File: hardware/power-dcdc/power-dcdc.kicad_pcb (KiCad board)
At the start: 2 copper layers, 110 x 70 mm, 67 parts, among them J1 SOLAR_IN, J2 BATT2, J3 BATT1, J4 DCDC-MEASURES, J5 DCDC-PWM, Q1 SIR164ADP, Q2 SIR164ADP, Q3 SI7149ADP, Q4 SI7149ADP, Q5 SI7149ADP, Q6 SI7149ADP, U1 LP4951C, U2 NCP5901B, U3 PAC1953-1, U4 DGD0215, U5 DGD0215

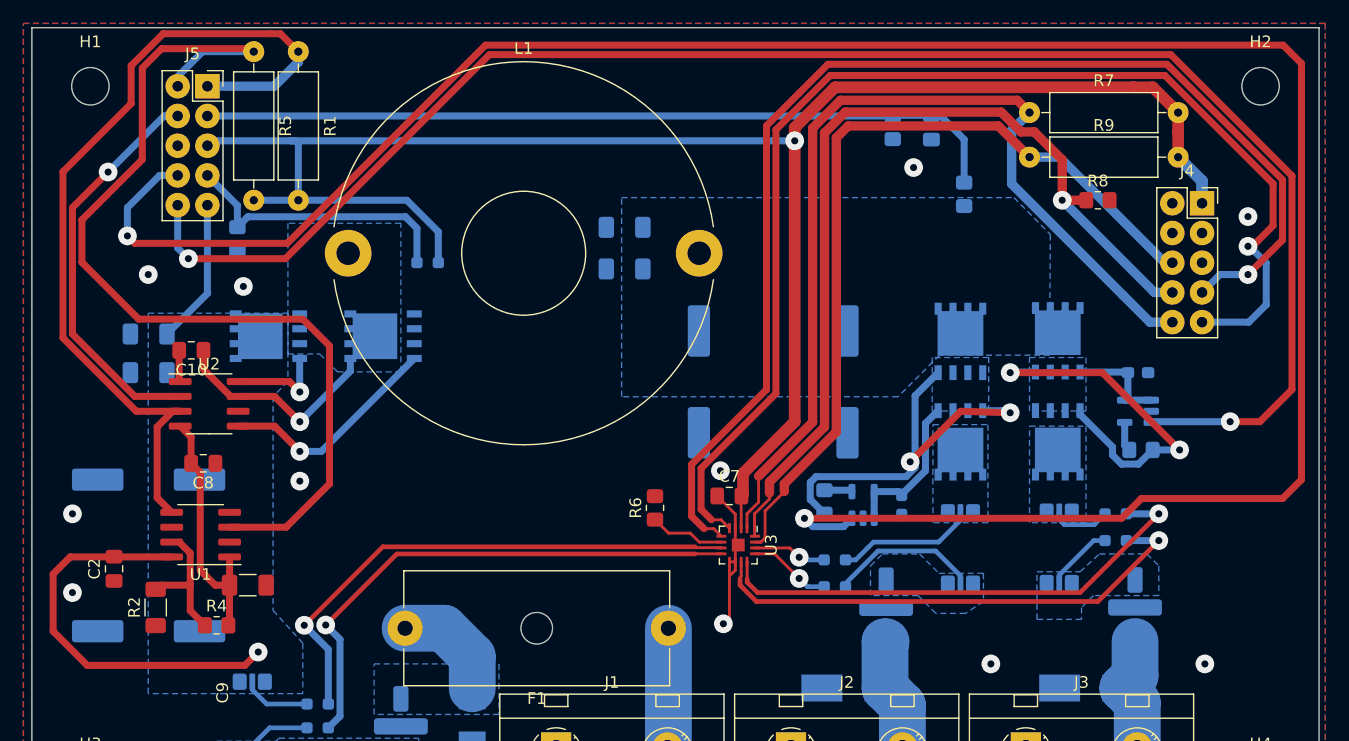
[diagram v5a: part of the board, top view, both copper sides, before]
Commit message: Make power tracks larger
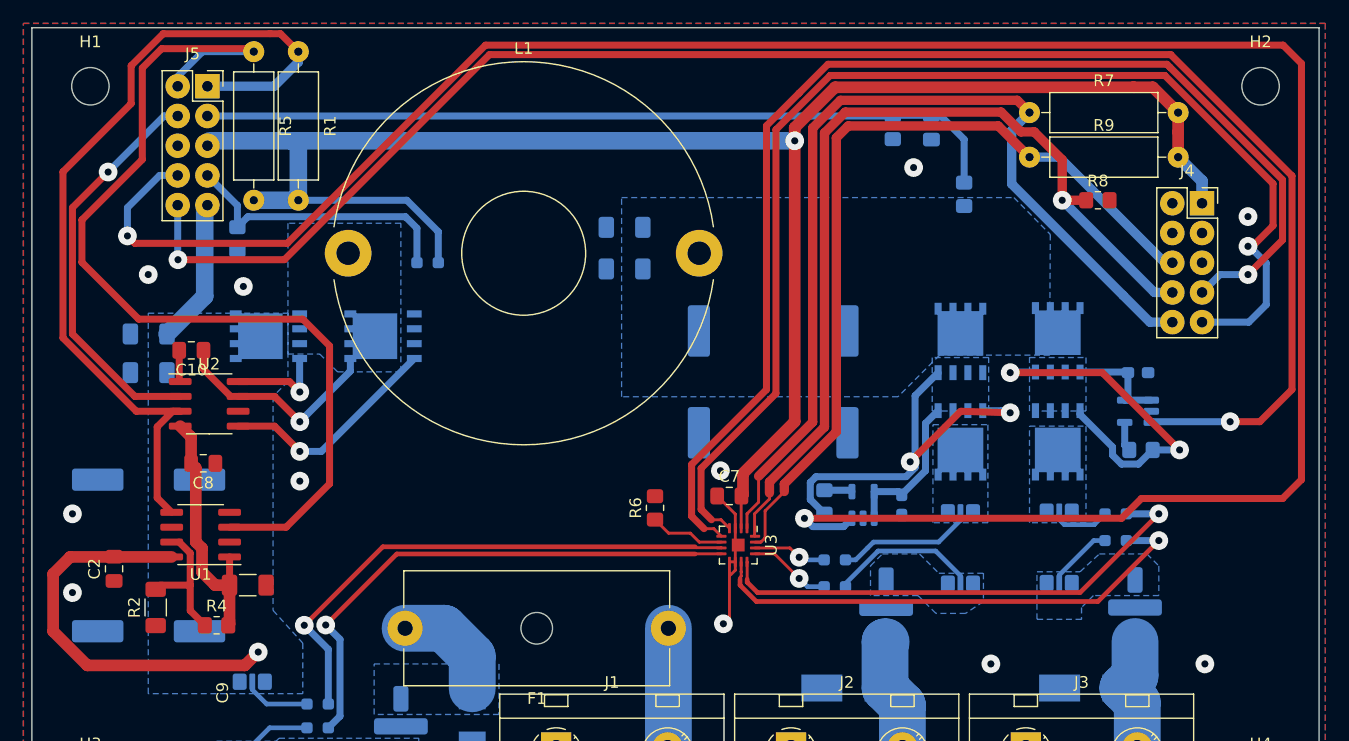
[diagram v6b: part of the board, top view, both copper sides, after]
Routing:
- net BATT1_ON: track 142.2 -> 142.9 mm
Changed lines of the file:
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@@
   (segment (start 110.771 119.8825) (end 110.6385 120.015) (width 1) (layer "F.Cu") (net 5))
   (via (at 115.189 89.662) (size 1.6) (drill 0.6) (layers "F.Cu" "B.Cu") (net 5))
-  (segment (start 72.136 89.662) (end 72.517 89.662) (width 0.6) (layer "B.Cu") (net 5))
-  (segment (start 72.517 89.662) (end 72.771 89.916) (width 0.6) (layer "B.Cu") (net 5))
+  (segment (start 72.136 89.662) (end 72.517 89.662) (width 1.5) (layer "B.Cu") (net 5))
+  (segment (start 72.517 89.662) (end 72.771 89.916) (width 1.5) (layer "B.Cu") (net 5))
   (segment (start 72.771 94.742) (end 82.042 94.742) (width 0.6) (layer "B.Cu") (net 5))
-  (segment (start 72.771 94.742) (end 68.961 94.742) (width 0.6) (layer "B.Cu") (net 5))
-  (segment (start 72.771 89.916) (end 72.771 94.742) (width 0.6) (layer "B.Cu") (net 5))
-  (segment (start 65.171 89.662) (end 72.136 89.662) (width 0.6) (layer "B.Cu") (net 5))
+  (segment (start 72.771 94.742) (end 68.961 94.742) (width 1.5) (layer "B.Cu") (net 5))
+  (segment (start 72.771 89.916) (end 72.771 94.742) (width 1.5) (layer "B.Cu") (net 5))
+  (segment (start 65.171 89.662) (end 72.136 89.662) (width 1.5) (layer "B.Cu") (net 5))
   (segment (start 150 93.104) (end 147.955 91.059) (width 1) (layer "B.Cu") (net 5))
-  (segment (start 115.189 89.662) (end 72.136 89.662) (width 0.6) (layer "B.Cu") (net 5))
+  (segment (start 115.189 89.662) (end 72.136 89.662) (width 1.5) (layer "B.Cu") (net 5))
   (segment (start 150 93.104) (end 150 95) (width 1) (layer "B.Cu") (net 5))
   (segment (start 84.7325 100.076) (end 84.7325 97.4325) (width 0.6) (layer "B.Cu") (net 5))
@@
   (segment (start 122.908 132.478) (end 123.002 132.478) (width 4) (layer "B.Cu") (net 8))
   (segment (start 124.394 141.506) (end 124.394 137.912) (width 4) (layer "B.Cu") (net 8))
-  (segment (start 53.2765 125.222) (end 61.946 125.222) (width 0.6) (layer "F.Cu") (net 9))
-  (segment (start 51.816 126.6825) (end 53.2765 125.222) (width 0.6) (layer "F.Cu") (net 9))
-  (segment (start 54.737 134.493) (end 51.816 131.572) (width 0.6) (layer "F.Cu") (net 9))
-  (segment (start 68.199 134.493) (end 54.737 134.493) (width 0.6) (layer "F.Cu") (net 9))
-  (segment (start 69.342 133.35) (end 68.199 134.493) (width 0.6) (layer "F.Cu") (net 9))
-  (segment (start 51.816 131.572) (end 51.816 126.6825) (width 0.6) (layer "F.Cu") (net 9))
+  (segment (start 53.2765 125.222) (end 61.946 125.222) (width 1) (layer "F.Cu") (net 9))
+  (segment (start 51.816 126.6825) (end 53.2765 125.222) (width 1) (layer "F.Cu") (net 9))
+  (segment (start 54.737 134.493) (end 51.816 131.572) (width 1) (layer "F.Cu") (net 9))
+  (segment (start 68.199 134.493) (end 54.737 134.493) (width 1) (layer "F.Cu") (net 9))
+  (segment (start 69.342 133.35) (end 68.199 134.493) (width 1) (layer "F.Cu") (net 9))
+  (segment (start 51.816 131.572) (end 51.816 126.6825) (width 1) (layer "F.Cu") (net 9))
   (via (at 69.342 133.35) (size 1.6) (drill 0.6) (layers "F.Cu" "B.Cu") (net 9))
-  (segment (start 65.024 102.693) (end 61.545 106.172) (width 0.6) (layer "B.Cu") (net 9))
-  (segment (start 65.024 102.693) (end 65 102.669) (width 0.6) (layer "B.Cu") (net 9))
-  (segment (start 65 102.669) (end 65 95.16) (width 0.6) (layer "B.Cu") (net 9))
-  (segment (start 66.8905 127.635) (end 65.659 127.635) (width 0.6) (layer "F.Cu") (net 10))
-  (segment (start 66.8905 130.9595) (end 66.786 131.064) (width 0.6) (layer "F.Cu") (net 10))
-  (segment (start 64.389 126.365) (end 64.389 118.0045) (width 0.6) (layer "F.Cu") (net 10))
-  (segment (start 65.659 127.635) (end 64.389 126.365) (width 0.6) (layer "F.Cu") (net 10))
-  (segment (start 66.8905 127.635) (end 66.8905 130.9595) (width 0.6) (layer "F.Cu") (net 10))
-  (segment (start 64.389 118.0045) (end 63.6055 117.221) (width 0.6) (layer "F.Cu") (net 10))
-  (segment (start 63.6055 117.221) (end 63.6055 114.9755) (width 0.6) (layer "F.Cu") (net 10))
-  (segment (start 63.6055 114.9755) (end 62.676 114.046) (width 0.6) (layer "F.Cu") (net 10))
+  (segment (start 61.545 106.172) (end 64.77 102.947) (width 1.5) (layer "B.Cu") (net 9))
+  (segment (start 64.77 102.947) (end 64.77 95.39) (width 1.5) (layer "B.Cu") (net 9))
+  (segment (start 64.77 95.39) (end 65 95.16) (width 1.5) (layer "B.Cu") (net 9))
+  (segment (start 65.659 127.635) (end 64.542 126.518) (width 1) (layer "F.Cu") (net 10))
+  (segment (start 64.542 126.518) (end 64.542 124.481263) (width 1) (layer "F.Cu") (net 10))
+  (segment (start 66.8905 130.9595) (end 66.786 131.064) (width 1) (layer "F.Cu") (net 10))
+  (segment (start 64.008 117.6235) (end 63.6055 117.221) (width 1) (layer "F.Cu") (net 10))
+  (segment (start 66.8905 127.635) (end 66.8905 130.9595) (width 1) (layer "F.Cu") (net 10))
+  (segment (start 64.008 123.947263) (end 64.008 117.6235) (width 1) (layer "F.Cu") (net 10))
+  (segment (start 63.6055 117.221) (end 63.6055 114.9755) (width 1) (layer "F.Cu") (net 10))
+  (segment (start 63.6055 114.9755) (end 62.676 114.046) (width 1) (layer "F.Cu") (net 10))
+  (segment (start 64.542 124.481263) (end 64.008 123.947263) (width 1) (layer "F.Cu") (net 10))
+  (segment (start 66.8905 127.635) (end 65.659 127.635) (width 1) (layer "F.Cu") (net 10))
   (segment (start 66.896 125.222) (end 66.896 127.6295) (width 0.6) (layer "F.Cu") (net 10))
   (segment (start 66.896 127.6295) (end 66.8905 127.635) (width 0.6) (layer "F.Cu") (net 10))
@@
   (segment (start 116.020463 121.922252) (end 116.731211 122.633) (width 0.6) (layer "B.Cu") (net 44))
   (segment (start 58.166 95.377) (end 60.923 92.62) (width 0.6) (layer "B.Cu") (net 44))
-  (segment (start 147.323615 82.296) (end 89.104132 82.296) (width 0.6) (layer "F.Cu") (net 45))
-  (segment (start 152.4 113.665) (end 154.94 113.665) (width 0.6) (layer "F.Cu") (net 45))
-  (segment (start 154.94 113.665) (end 157.686 110.919) (width 0.6) (layer "F.Cu") (net 45))
-  (segment (start 157.686 92.658385) (end 147.323615 82.296) (width 0.6) (layer "F.Cu") (net 45))
-  (segment (start 89.104132 82.296) (end 71.665632 99.7345) (width 0.6) (layer "F.Cu") (net 45))
-  (segment (start 71.665632 99.7345) (end 63.373 99.7345) (width 0.6) (layer "F.Cu") (net 45))
-  (segment (start 157.686 110.919) (end 157.686 92.658385) (width 0.6) (layer "F.Cu") (net 45))
+  (segment (start 71.578132 99.822) (end 89.104132 82.296) (width 0.6) (layer "F.Cu") (net 45))
+  (segment (start 62.484 99.822) (end 71.578132 99.822) (width 0.6) (layer "F.Cu") (net 45))
+  (segment (start 147.323615 82.296) (end 157.686 92.658385) (width 0.6) (layer "F.Cu") (net 45))
+  (segment (start 157.686 110.919) (end 154.94 113.665) (width 0.6) (layer "F.Cu") (net 45))
+  (segment (start 154.94 113.665) (end 152.4 113.665) (width 0.6) (layer "F.Cu") (net 45))
+  (segment (start 89.104132 82.296) (end 147.323615 82.296) (width 0.6) (layer "F.Cu") (net 45))
+  (segment (start 157.686 92.658385) (end 157.686 110.919) (width 0.6) (layer "F.Cu") (net 45))
   (via (at 152.4 113.665) (size 1.6) (drill 0.6) (layers "F.Cu" "B.Cu") (net 45))
-  (via (at 63.373 99.7345) (size 1.6) (drill 0.6) (layers "F.Cu" "B.Cu") (net 45))
+  (via (at 62.484 99.822) (size 1.6) (drill 0.6) (layers "F.Cu" "B.Cu") (net 45))
   (segment (start 145.7245 113.665) (end 145.6635 113.726) (width 0.6) (layer "B.Cu") (net 45))
+  (segment (start 62.46 99.798) (end 62.46 95.16) (width 0.6) (layer "B.Cu") (net 45))
   (segment (start 152.4 113.665) (end 145.7245 113.665) (width 0.6) (layer "B.Cu") (net 45))
-  (segment (start 62.46 95.16) (end 62.46 98.8215) (width 0.6) (layer "B.Cu") (net 45))
-  (segment (start 62.46 98.8215) (end 63.373 99.7345) (width 0.6) (layer "B.Cu") (net 45))
+  (segment (start 62.484 99.822) (end 62.46 99.798) (width 0.6) (layer "B.Cu") (net 45))
   (segment (start 52.657 106.507512) (end 58.925488 112.776) (width 0.6) (layer "F.Cu") (net 46))
   (segment (start 61.222 80.51) (end 58.4835 83.2485) (width 0.6) (layer "F.Cu") (net 46))

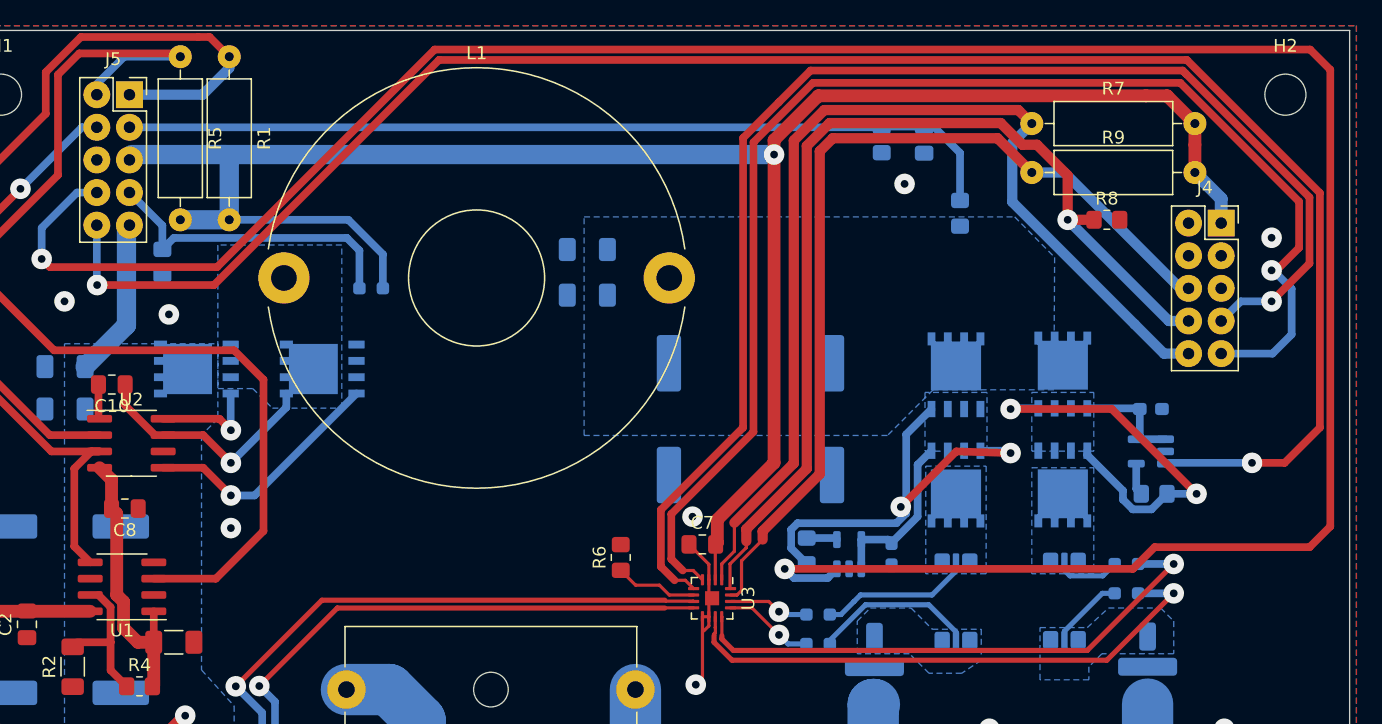
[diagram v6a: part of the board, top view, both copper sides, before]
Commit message: Re-route PCBs to move RJ45 connectors on bottom, saving a bit of stack size.
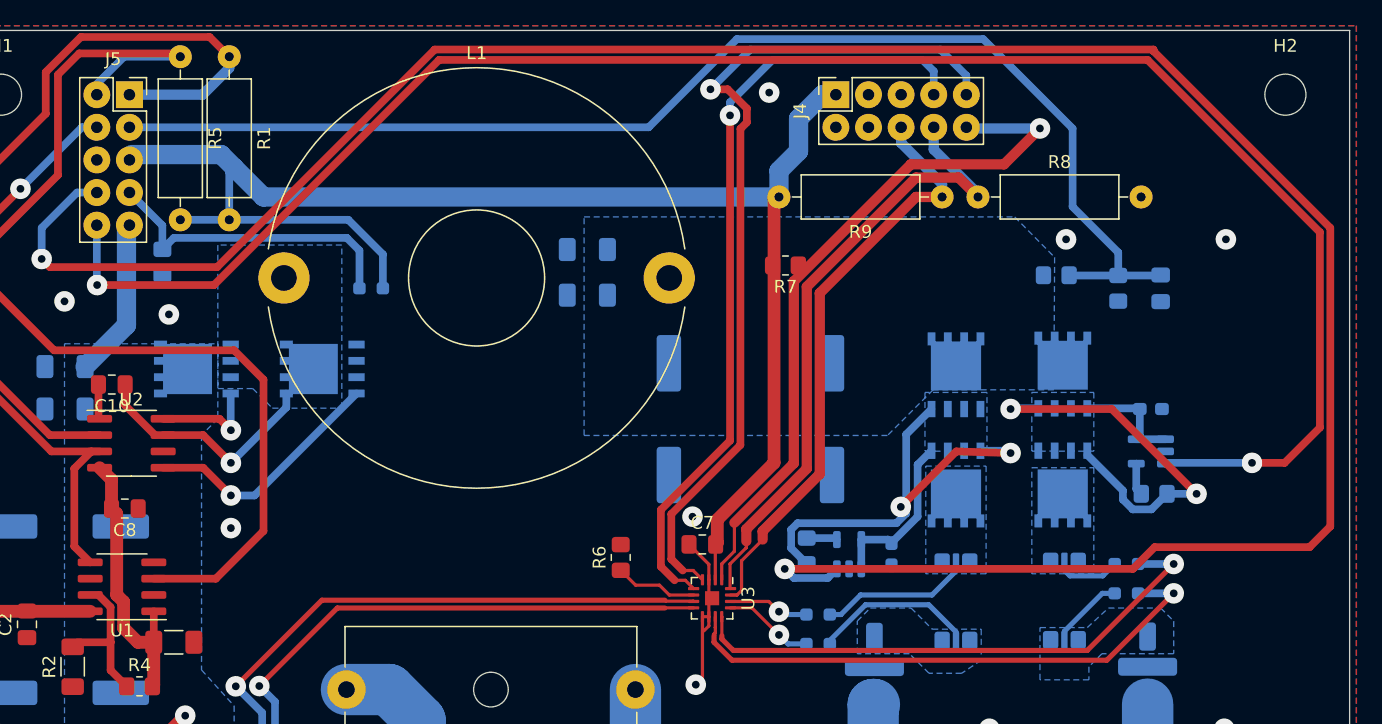
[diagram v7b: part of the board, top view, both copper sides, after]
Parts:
- R7: footprint Resistor_THT:R_Axial_DIN0309_L9.0mm_D3.2mm_P12.70mm_Horizontal -> Resistor_SMD:R_0805_2012Metric_Pad1.20x1.40mm_HandSolder
- R8: footprint Resistor_SMD:R_0805_2012Metric_Pad1.20x1.40mm_HandSolder -> Resistor_THT:R_Axial_DIN0309_L9.0mm_D3.2mm_P12.70mm_Horizontal
- moved J4 31.6 mm to (120.0, 85.0), turned to 90 degrees
- moved R7 22.1 mm to (116.1, 98.3), turned to 180 degrees
- moved C19 21.7 mm to (145.3, 100.1)
- moved R15 21.7 mm to (142.0, 100.1)
- moved R8 10.2 mm to (131.1, 93.0)
- moved R14 8.91 mm to (137.2, 99.1), turned to 0 degrees
- moved R9 7.24 mm to (128.3, 93.0), turned to 180 degrees
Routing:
- net /SDA: track 103.5 -> 61.1 mm
- net +5V: track 155.1 -> 117.7 mm, vias 1 -> 0
- net /SCL: track 104.7 -> 67.6 mm
- net PWM_V: track 69.2 -> 99.1 mm
- net /~{PAC_DOWN}: track 77.9 -> 50.1 mm, vias 1 -> 0
- net /AL1: track 81.8 -> 55.3 mm, vias 0 -> 1
- net /AL2: track 71.7 -> 46.0 mm
- net BATT2_ON: track 200.2 -> 193.0 mm
- net BATT1_ON: track 142.9 -> 141.1 mm
- net GND: track 13.7 -> 13.0 mm, vias 12 -> 13
- net /PWM_OK: track 74.2 -> 73.6 mm
